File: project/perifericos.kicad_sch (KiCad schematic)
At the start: 68 parts, among them P1 Conector SMD 2x10, P2 Conector SMD 2x10, P3 Conector SMD 2x10, P4 Conector SMD 2x10, SW1 SW_Push, SW2 SW_Push, SW3 SW_Push, SW4 SW_Push, SW5 SW_Push, SW6 SW_Push, SW7 SW_Push, SW8 SW_Push, U6 ICE40HX4K-TQ144, Y2 ECS-3225MVQ-1000-CN-TR

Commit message: Agregados footprints de todos los componentes
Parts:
- D10, D11, D12, D9: value LED -> LED Red; footprint (none) -> 150141RS73100(LED):LEDM3528X210N
- D5, D6, D7, D8: value LED -> LED Green; footprint (none) -> 150141RS73100(LED):LEDM3528X210N
- SW1, SW2, SW3, SW4, SW5, SW6, SW7, SW8: footprint (none) -> TS04_66_75_BK_100_SMT:SW_TS04-66-75-BK-100-SMT
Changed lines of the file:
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@@
 			)
 		)
-		(property "Value" "LED"
+		(property "Value" "LED Green"
 			(at 139.7 54.9274 90)
 			(effects
@@
 			)
 		)
-		(property "Footprint" ""
+		(property "Footprint" "150141RS73100(LED):LEDM3528X210N"
 			(at 135.89 52.07 0)
 			(effects
@@
 			)
 		)
-		(property "Value" "LED"
+		(property "Value" "LED Red"
 			(at 162.56 54.9274 90)
 			(effects
@@
 			)
 		)
-		(property "Footprint" ""
+		(property "Footprint" "150141RS73100(LED):LEDM3528X210N"
 			(at 158.75 52.07 0)
 			(effects
@@
 	)
 	(symbol
+		(lib_name "SW_Push_1")
 		(lib_id "Switch:SW_Push")
 		(at 245.11 101.6 90)
@@
 			)
 		)
-		(property "Footprint" ""
+		(property "Footprint" "TS04_66_75_BK_100_SMT:SW_TS04-66-75-BK-100-SMT"
 			(at 240.03 101.6 0)
 			(effects
@@
 		)
 		(property "Description" "Push button switch, generic, two pins"
-			(at 245.11 101.6 0)
+			(at 249.428 101.6 0)
 			(effects
 				(font
@@
 			)
 		)
-		(property "Footprint" ""
+		(property "Footprint" "TS04_66_75_BK_100_SMT:SW_TS04-66-75-BK-100-SMT"
 			(at 220.98 101.6 0)
 			(effects
@@
 			)
 		)
-		(property "Footprint" ""
+		(property "Footprint" "TS04_66_75_BK_100_SMT:SW_TS04-66-75-BK-100-SMT"
 			(at 163.83 101.6 0)
 			(effects
@@
 			)
 		)
-		(property "Footprint" ""
+		(property "Footprint" "TS04_66_75_BK_100_SMT:SW_TS04-66-75-BK-100-SMT"
 			(at 201.93 101.6 0)
 			(effects
@@
 			)
 		)
-		(property "Footprint" ""
+		(property "Footprint" "TS04_66_75_BK_100_SMT:SW_TS04-66-75-BK-100-SMT"
 			(at 144.78 101.6 0)
 			(effects
@@
 			)
 		)
-		(property "Value" "LED"
+		(property "Value" "LED Red"
 			(at 158.75 54.9274 90)
 			(effects
@@
 			)
 		)
-		(property "Footprint" ""
+		(property "Footprint" "150141RS73100(LED):LEDM3528X210N"
 			(at 154.94 52.07 0)
 			(effects
@@
 			)
 		)
-		(property "Value" "LED"
+		(property "Value" "LED Green"
 			(at 147.32 54.9274 90)
 			(effects
@@
 			)
 		)
-		(property "Footprint" ""
+		(property "Footprint" "150141RS73100(LED):LEDM3528X210N"
 			(at 143.51 52.07 0)
 			(effects
@@
 			)
 		)
-		(property "Value" "LED"
+		(property "Value" "LED Red"
 			(at 151.13 54.9274 90)
 			(effects
@@
 			)
 		)
-		(property "Footprint" ""
+		(property "Footprint" "150141RS73100(LED):LEDM3528X210N"
 			(at 147.32 52.07 0)
 			(effects
@@
 			)
 		)
-		(property "Footprint" ""
+		(property "Footprint" "TS04_66_75_BK_100_SMT:SW_TS04-66-75-BK-100-SMT"
 			(at 182.88 101.6 0)
 			(effects
@@
 			)
 		)
-		(property "Value" "LED"
+		(property "Value" "LED Green"
 			(at 135.89 54.9274 90)
 			(effects
@@
 			)
 		)
-		(property "Footprint" ""
+		(property "Footprint" "150141RS73100(LED):LEDM3528X210N"
 			(at 132.08 52.07 0)
 			(effects
@@
 			)
 		)
-		(property "Value" "LED"
+		(property "Value" "LED Green"
 			(at 143.51 54.9274 90)
 			(effects
@@
 			)
 		)
-		(property "Footprint" ""
+		(property "Footprint" "150141RS73100(LED):LEDM3528X210N"
 			(at 139.7 52.07 0)
 			(effects
@@
 			)
 		)
-		(property "Footprint" ""
+		(property "Footprint" "TS04_66_75_BK_100_SMT:SW_TS04-66-75-BK-100-SMT"
 			(at 125.73 101.6 0)
 			(effects
@@
 			)
 		)
-		(property "Value" "LED"
+		(property "Value" "LED Red"
 			(at 154.94 54.9274 90)
 			(effects
@@
 			)
 		)
-		(property "Footprint" ""
+		(property "Footprint" "150141RS73100(LED):LEDM3528X210N"
 			(at 151.13 52.07 0)
 			(effects
@@
 			)
 		)
-		(property "Footprint" ""
+		(property "Footprint" "TS04_66_75_BK_100_SMT:SW_TS04-66-75-BK-100-SMT"
 			(at 259.08 101.6 0)
 			(effects

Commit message: PCB etapa de potencia y comunicacion lista
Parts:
- renumbered TP7 to TP3
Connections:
- net LED1: now also U6.37 (IOB_56); no longer U6.110 (IOT_168)
- net LED2: now also U6.38 (IOB_57); no longer U6.112 (IOT_169)
- net LED3: now also U6.39 (IOB_61); no longer U6.113 (IOT_170)
- net LED4: now also U6.41 (IOB_63); no longer U6.114 (IOT_171)
- net LED5: now also U6.42 (IOB_64); no longer U6.115 (IOT_172)
- net LED6: now also U6.43 (IOB_71); no longer U6.116 (IOT_173)
- net LED7: now also U6.44 (IOB_72); no longer U6.117 (IOT_174)
- net LED8: now also U6.45 (IOB_73); no longer U6.118 (IOT_177)
- no-connect marks 22 -> 20
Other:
- moved on the sheet: C42, TP3, Y2

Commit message: Version 1 pcb, sin finalizar
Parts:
- removed TP3: 100MHZ, TestPoint:TestPoint_Pad_D2.5mm, symbol Connector:TestPoint
- P1, P2, P3, P4: footprint FRT-FPGA:Header 2x10 SMD -> Connector_PinSocket_2.54mm:PinSocket_2x10_P2.54mm_Vertical
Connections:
- net +3V3: now also P1.1 (3V3), P1.2 (3V3), P2.1 (3V3), P2.2 (3V3), P3.1 (3V3), P3.2 (3V3), P4.1 (3V3), P4.2 (3V3); no longer P1.3V3, P1.3V3_2 (3V3), P2.3V3, P2.3V3_2 (3V3), P3.3V3, P3.3V3_2 (3V3), P4.3V3, P4.3V3_2 (3V3)
- net +5V: now also P1.3 (5V), P1.4 (5V), P2.3 (5V), P2.4 (5V), P3.3 (5V), P3.4 (5V), P4.3 (5V), P4.4 (5V); no longer P1.5V, P1.5V_2 (5V), P2.5V, P2.5V_2 (5V), P3.5V, P3.5V_2 (5V), P4.5V, P4.5V_2 (5V)
- net 12MHz_CLK: now also U6.129 (IOT_198_GBIN0); no longer U6.52 (IOB_82_GBIN4)
- net BOT1: now also U6.37 (IOB_56); no longer U6.144 (IOT_222)
- net BOT2: now also U6.38 (IOB_57); no longer U6.143 (IOT_221)
- net BOT3: now also U6.39 (IOB_61); no longer U6.142 (IOT_220)
- net BOT4: now also U6.41 (IOB_63); no longer U6.141 (IOT_219)
- net BOT5: now also U6.42 (IOB_64); no longer U6.139 (IOT_217)
- net BOT6: now also U6.43 (IOB_71); no longer U6.138 (IOT_216)
- net BOT7: now also U6.44 (IOB_72); no longer U6.137 (IOT_215)
- net BOT8: now also U6.45 (IOB_73); no longer U6.136 (IOT_214)
- net GND: now also P1.19 (GND), P1.20 (GND), P2.19 (GND), P2.20 (GND), P3.19 (GND), P3.20 (GND), P4.19 (GND), P4.20 (GND); no longer P1.GND, P1.GND_2 (GND), P2.GND, P2.GND_2 (GND), P3.GND, P3.GND_2 (GND), P4.GND, P4.GND_2 (GND)
- net LED1: now also U6.110 (IOT_168); no longer U6.37 (IOB_56)
- net LED2: now also U6.112 (IOT_169); no longer U6.38 (IOB_57)
- net LED3: now also U6.113 (IOT_170); no longer U6.39 (IOB_61)
- net LED4: now also U6.114 (IOT_171); no longer U6.41 (IOB_63)
- net LED5: now also U6.115 (IOT_172); no longer U6.42 (IOB_64)
- net LED6: now also U6.116 (IOT_173); no longer U6.43 (IOB_71)
- net LED7: now also U6.117 (IOT_174); no longer U6.44 (IOB_72)
- net LED8: now also U6.118 (IOT_177); no longer U6.45 (IOB_73)
- net at U6.91 (IOR_139): now also P4.5 (IO1); no longer P4.IO1
- net at U6.102 (IOR_161): now also P4.14 (IO10); no longer P4.IO10
- net at U6.104 (IOR_164): now also P4.15 (IO11); no longer P4.IO11
- net at U6.105 (IOR_165): now also P4.16 (IO12); no longer P4.IO12
- net at U6.106 (IOR_166): now also P4.17 (IO13); no longer P4.IO13
- net at U6.107 (IOR_167): now also P4.18 (IO14); no longer P4.IO14
- net at U6.93 (IOR_140_GBIN3): now also P4.6 (IO2); no longer P4.IO2
- net at U6.94 (IOR_141_GBIN2): now also P4.7 (IO3); no longer P4.IO3
- net at U6.95 (IOR_144): now also P4.8 (IO4); no longer P4.IO4
- net at U6.96 (IOR_146): now also P4.9 (IO5); no longer P4.IO5
- net at U6.97 (IOR_147): now also P4.10 (IO6); no longer P4.IO6
- net at U6.98 (IOR_148): now also P4.11 (IO7); no longer P4.IO7
- net at U6.99 (IOR_152): now also P4.12 (IO8); no longer P4.IO8
- net at U6.101 (IOR_160): now also P4.13 (IO9); no longer P4.IO9
- net at U6.1 (IOL_2A): now also P1.5 (IO1); no longer P1.IO1
- net at U6.10 (IOL_5B): now also P1.12 (IO8); no longer P1.IO8
- net at U6.11 (IOL_8A): now also P1.13 (IO9); no longer P1.IO9
- net at U6.12 (IOL_8B): now also P1.14 (IO10); no longer P1.IO10
- net at U6.15 (IOL_10A): now also P1.15 (IO11); no longer P1.IO11
- net at U6.16 (IOL_10B): now also P1.16 (IO12); no longer P1.IO12
- net at U6.17 (IOL_12A): now also P1.17 (IO13); no longer P1.IO13
- net at U6.18 (IOL_12B): now also P1.18 (IO14); no longer P1.IO14
- net at U6.19 (IOL_13A): now also P2.5 (IO1); no longer P2.IO1
- net at U6.2 (IOL_2B): now also P1.6 (IO2); no longer P1.IO2
- net at U6.20 (IOL_13B_GBIN7): now also P2.6 (IO2); no longer P2.IO2
- net at U6.21 (IOL_14A_GBIN6): now also P2.7 (IO3); no longer P2.IO3
- net at U6.22 (IOL_14B): now also P2.8 (IO4); no longer P2.IO4
- net at U6.23 (IOL_17A): now also P2.9 (IO5); no longer P2.IO5
- net at U6.24 (IOL_17B): now also P2.10 (IO6); no longer P2.IO6
- net at U6.25 (IOL_18A): now also P2.11 (IO7); no longer P2.IO7
- net at U6.26 (IOL_18B): now also P2.12 (IO8); no longer P2.IO8
- net at U6.28 (IOL_23A): now also P2.13 (IO9); no longer P2.IO9
- net at U6.29 (IOL_23B): now also P2.14 (IO10); no longer P2.IO10
- net at U6.3 (IOL_3A): now also P1.7 (IO3); no longer P1.IO3
- net at U6.31 (IOL_24A): now also P2.15 (IO11); no longer P2.IO11
- net at U6.32 (IOL_24B): now also P2.16 (IO12); no longer P2.IO12
- net at U6.33 (IOL_25A): now also P2.17 (IO13); no longer P2.IO13
- net at U6.34 (IOL_25B): now also P2.18 (IO14); no longer P2.IO14
- net at U6.4 (IOL_3B): now also P1.8 (IO4); no longer P1.IO4
- net at U6.7 (IOL_4A): now also P1.9 (IO5); no longer P1.IO5
- net at U6.8 (IOL_4B): now also P1.10 (IO6); no longer P1.IO6
- net at U6.9 (IOL_5A): now also P1.11 (IO7); no longer P1.IO7
- net at U6.73 (IOR_109): now also P3.5 (IO1); no longer P3.IO1
- net at U6.83 (IOR_119): now also P3.14 (IO10); no longer P3.IO10
- net at U6.84 (IOR_120): now also P3.15 (IO11); no longer P3.IO11
- net at U6.85 (IOR_128): now also P3.16 (IO12); no longer P3.IO12
- net at U6.87 (IOR_136): now also P3.17 (IO13); no longer P3.IO13
- net at U6.88 (IOR_137): now also P3.18 (IO14); no longer P3.IO14
- net at U6.74 (IOR_110): now also P3.6 (IO2); no longer P3.IO2
- net at U6.75 (IOR_111): now also P3.7 (IO3); no longer P3.IO3
- net at U6.76 (IOR_112): now also P3.8 (IO4); no longer P3.IO4
- net at U6.78 (IOR_114): now also P3.9 (IO5); no longer P3.IO5
- net at U6.79 (IOR_115): now also P3.10 (IO6); no longer P3.IO6
- net at U6.80 (IOR_116): now also P3.11 (IO7); no longer P3.IO7
- net at U6.81 (IOR_117): now also P3.12 (IO8); no longer P3.IO8
- net at U6.82 (IOR_118): now also P3.13 (IO9); no longer P3.IO9
- no-connect marks 20 -> 14

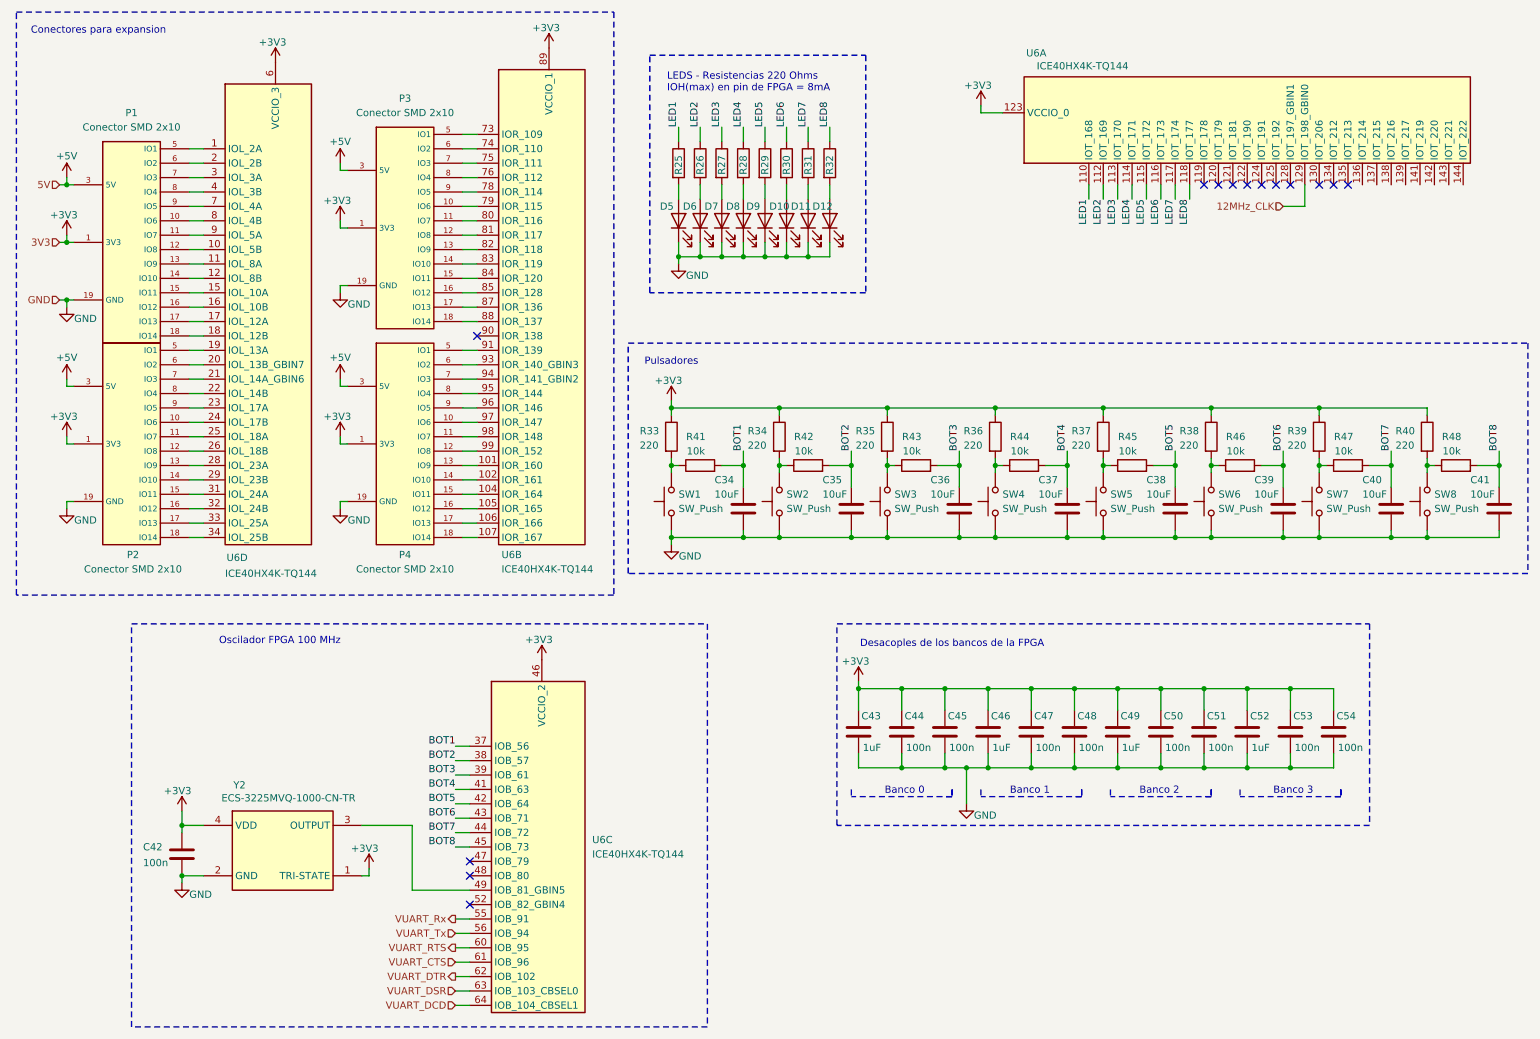
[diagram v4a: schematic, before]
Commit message: Agregado de datasheets, cambio de regulador zener, ajuste de posicion de regulador, modelo 3d de oscilador
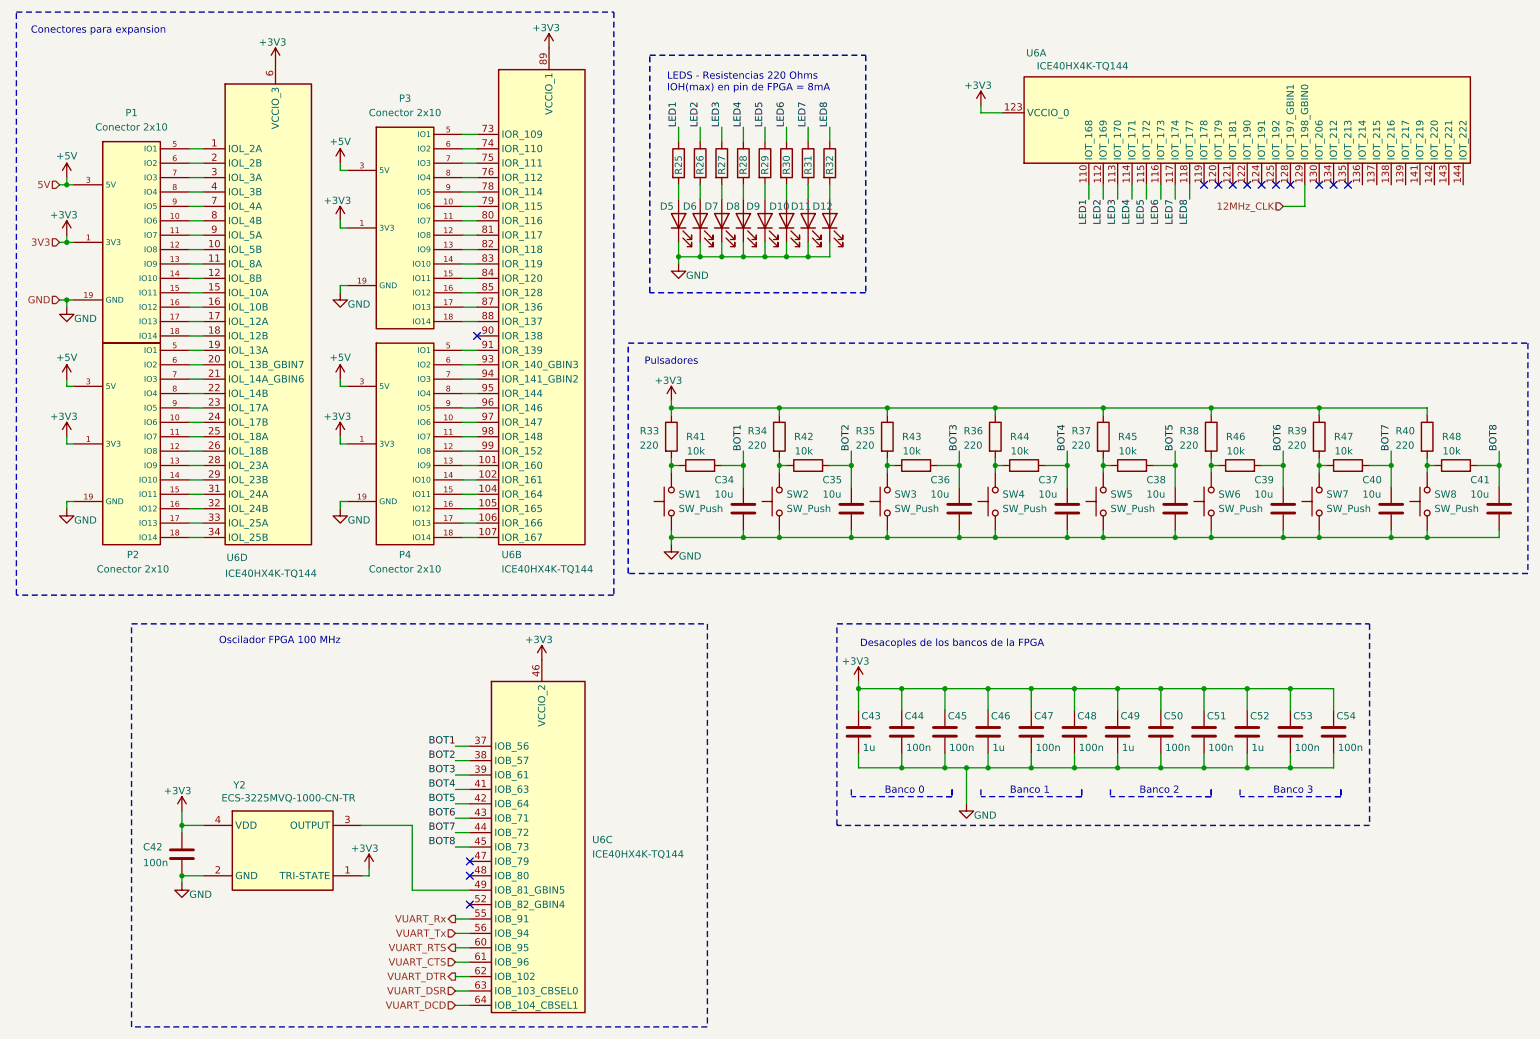
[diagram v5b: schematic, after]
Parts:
- C34, C35, C36, C37, C38, C39, C40, C41: value 10uF -> 10u; Código del fabricante (Order Code) (none) -> CL31B106KAHNNNE; Código del vendedor (Provider Order Code) (none) -> 187-CL31B106KAHNNNE; Fabricante (none) -> Samsung; Package (none) -> 1206
- C42, C44, C45, C47, C48, C50, C51, C53, C54: Código del fabricante (Order Code) (none) -> CL31B104KBCNFNC; Código del vendedor (Provider Order Code) (none) -> 187-CL31B104KBCNFNC; Fabricante (none) -> Samsung; Package (none) -> 1206
- C43, C46, C49, C52: value 1uF -> 1u; Código del fabricante (Order Code) (none) -> CL31B105KAHNFNE; Código del vendedor (Provider Order Code) (none) -> 187-CL31B105KAHNFNE; Fabricante (none) -> Samsung; Package (none) -> 1206
- D10, D11, D12, D9: value LED Red -> LED Green; Código del fabricante (Order Code) (none) -> 150141GS73100; Código del vendedor (Provider Order Code) (none) -> 710-150141GS73100; Fabricante (none) -> Wurth Elektronik; Package (none) -> 3528
- D5, D6, D7, D8: Código del fabricante (Order Code) (none) -> 150141GS73100; Código del vendedor (Provider Order Code) (none) -> 710-150141GS73100; Fabricante (none) -> Wurth Elektronik; Package (none) -> 3528
- P1, P2, P3, P4: value Conector SMD 2x10 -> Conector 2x10
- R25, R26, R27, R28, R29, R30, R31, R32: value R -> 220; Código del fabricante (Order Code) (none) -> RC1206FR-13220RL; Código del vendedor (Provider Order Code) (none) -> 603-RC1206FR-13220RL; Fabricante (none) -> Yageo; Package (none) -> 1206
- R33, R34, R35, R36, R37, R38, R39, R40: Código del fabricante (Order Code) (none) -> RC1206FR-13220RL; Código del vendedor (Provider Order Code) (none) -> 603-RC1206FR-13220RL; Fabricante (none) -> Yageo; Package (none) -> 1206
- R41, R42, R43, R44, R45, R46, R47, R48: Código del fabricante (Order Code) (none) -> AC1206FR-0710KL; Código del vendedor (Provider Order Code) (none) -> 603-AC1206FR-0710KL; Fabricante (none) -> Yageo; Package (none) -> 1206
- SW1, SW2, SW3, SW4, SW5, SW6, SW7, SW8: Código del fabricante (Order Code) (none) -> TS04-66-75-BK-100-SMT; Código del vendedor (Provider Order Code) (none) -> 179-TS04-66-75-BK-100-SMT; Fabricante (none) -> Same sky; Package (none) -> SPST
- U6: Código del fabricante (Order Code) (none) -> iCE40HX4K-TQ144; Código del vendedor (Provider Order Code) (none) -> 842-iCE40HX4K-TQ144; Fabricante (none) -> Lattice Semiconductor; Package (none) -> TQFP-144
- Y2: Código del fabricante (Order Code) (none) -> ECS-3225MVQ-1000-CN-TR; Código del vendedor (Provider Order Code) (none) -> 520-ECS-3225MVQ-1000-CN-TR; Fabricante (none) -> ECS INC; Height 1.2 -> (none); Manufacturer_Name ECS -> (none); Manufacturer_Part_Number ECS-3225MVQ-1000-CN-TR -> (none); Mouser Part Number 520-3225MVQ-1000CN-T -> (none); Mouser Price/Stock https://www.mouser.co.uk/ProductDetail/ECS/ECS-3225MVQ-1000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 -> (none); Package (none) -> 3225

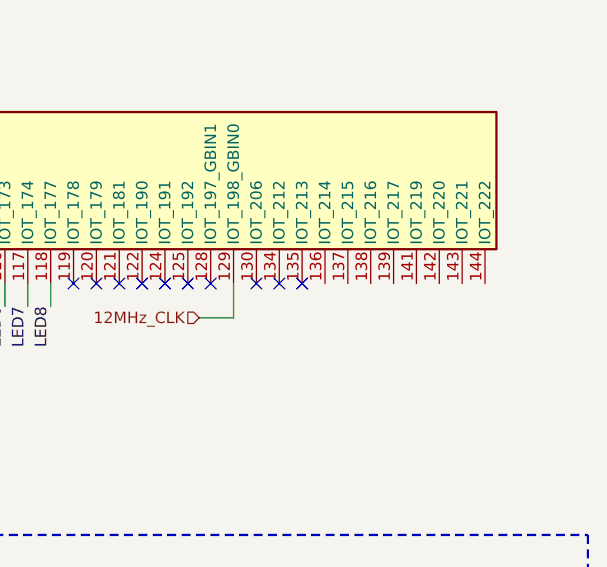
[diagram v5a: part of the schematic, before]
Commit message: Correcion de errores ERC y DRC, avisos ERC y DRC, correccion de huellas, silksreens pisando soldermask, etc
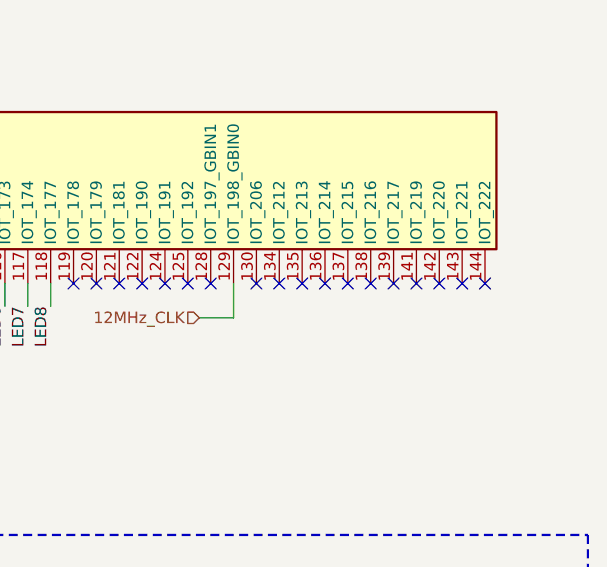
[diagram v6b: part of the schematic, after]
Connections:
- no-connect marks 14 -> 22
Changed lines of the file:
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@@
+	)
+	(no_connect
+		(at 260.35 45.72)
+	)
+	(no_connect
+		(at 265.43 45.72)
+	)
+	(no_connect
+		(at 267.97 45.72)
+	)
+	(no_connect
+		(at 255.27 45.72)
 	)
 	(no_connect
@@
 	)
 	(no_connect
+		(at 262.89 45.72)
+	)
+	(no_connect
 		(at 247.65 45.72)
 	)
 	(no_connect
 		(at 95.25 172.72)
+	)
+	(no_connect
+		(at 252.73 45.72)
+	)
+	(no_connect
+		(at 270.51 45.72)
 	)
 	(no_connect
@@
 		(at 237.49 45.72)
 	)
+	(no_connect
+		(at 257.81 45.72)
+	)
 	(wire
